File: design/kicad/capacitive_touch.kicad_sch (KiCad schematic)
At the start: 65 parts, among them J10 Conn_01x09_Pin, J2 Conn_01x09_Pin, J4 Conn_01x09_Socket, J5 Conn_01x09_Socket, J6 Conn_01x09_Socket, J7 Conn_01x09_Socket, J8 Conn_01x09_Pin, J9 Conn_01x09_Pin, U4 MPR121QR2, U5 MPR121QR2, U6 MPR121QR2

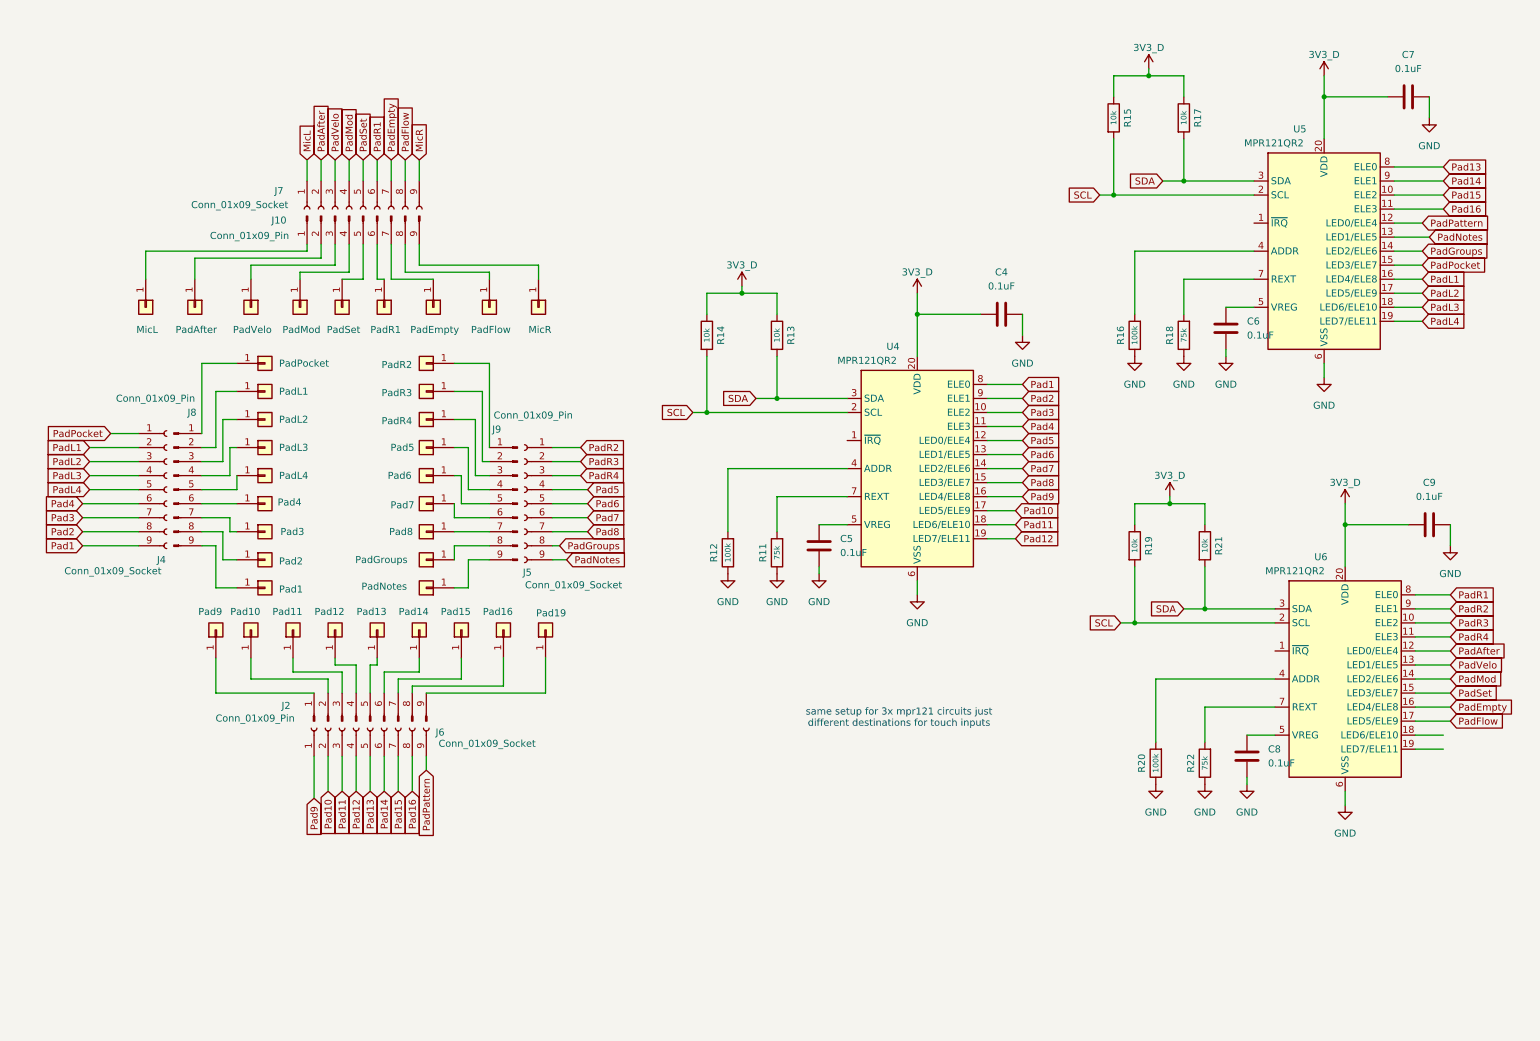
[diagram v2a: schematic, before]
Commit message: completes kicad schematic, starts pcb layout
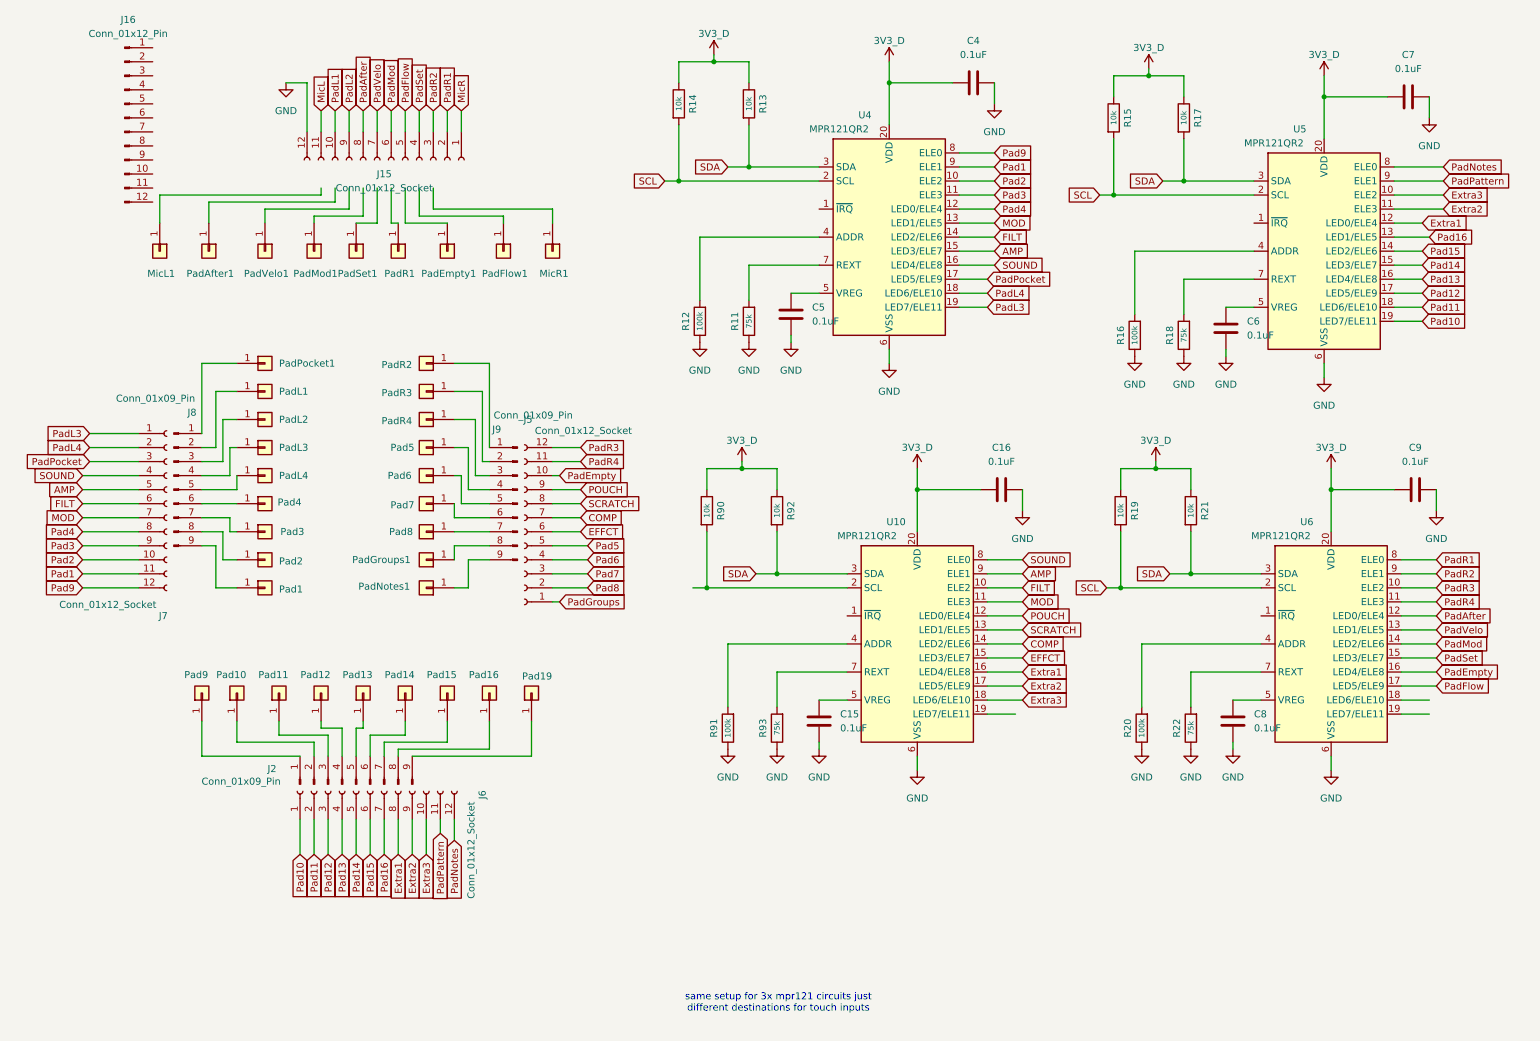
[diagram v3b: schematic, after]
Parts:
- removed J10: Conn_01x09_Pin, symbol Connector:Conn_01x09_Pin
- removed J4, J5, J6, J7: Conn_01x09_Socket, symbol Connector:Conn_01x09_Socket
- added C15, C16: 0.1uF, Capacitor_SMD:C_0402_1005Metric, symbol Device:C
- added J15, J5, J6, J7: Conn_01x12_Socket, Connector_PinSocket_1.27mm:PinSocket_1x12_P1.27mm_Vertical, symbol Connector:Conn_01x12_Socket
- added J16: Conn_01x12_Pin, Connector_PinHeader_1.27mm:PinHeader_1x12_P1.27mm_Vertical_SMD_Pin1Left, symbol Connector:Conn_01x12_Pin
- added R90, R92: 10k, Resistor_SMD:R_0603_1608Metric, symbol Device:R
- added R91: 100k, Resistor_SMD:R_0603_1608Metric, symbol Device:R
- added R93: 75k, Resistor_SMD:R_0603_1608Metric, symbol Device:R
- added U10: MPR121QR2, Package_DFN_QFN:UQFN-20_3x3mm_P0.4mm, symbol Sensor_Touch:MPR121QR2
- C4, C7, C9: footprint Capacitor_SMD:C_0603_1608Metric -> Capacitor_SMD:C_0402_1005Metric; LCSC (none) -> C1525
- C5, C6, C8: footprint Capacitor_SMD:C_0603_1608Metric -> Capacitor_SMD:C_0402_1005Metric; LCSC C6119867 -> C1525
- J2, J8, J9: footprint (none) -> Connector_PinHeader_1.27mm:PinHeader_1x09_P1.27mm_Vertical_SMD_Pin1Left
- MicL1: renamed from MicL; footprint (none) -> TestPoint:TestPoint_Pad_2.5x2.5mm
- MicR1: renamed from MicR; footprint (none) -> TestPoint:TestPoint_Pad_2.5x2.5mm
- Pad1, Pad10, Pad11, Pad12, Pad13, Pad14, Pad15, Pad16, Pad19, Pad2, Pad3, Pad4, Pad5, Pad6, Pad7, Pad8, Pad9, PadL1, PadL2, PadL3, PadL4, PadR1, PadR2, PadR3, PadR4: footprint (none) -> TestPoint:TestPoint_Pad_2.5x2.5mm
- PadAfter1: renamed from PadAfter; footprint (none) -> TestPoint:TestPoint_Pad_2.5x2.5mm
- PadEmpty1: renamed from PadEmpty; footprint (none) -> TestPoint:TestPoint_Pad_2.5x2.5mm
- PadFlow1: renamed from PadFlow; footprint (none) -> TestPoint:TestPoint_Pad_2.5x2.5mm
- PadGroups1: renamed from PadGroups; footprint (none) -> TestPoint:TestPoint_Pad_2.5x2.5mm
- PadMod1: renamed from PadMod; footprint (none) -> TestPoint:TestPoint_Pad_2.5x2.5mm
- PadNotes1: renamed from PadNotes; footprint (none) -> TestPoint:TestPoint_Pad_2.5x2.5mm
- PadPocket1: renamed from PadPocket; footprint (none) -> TestPoint:TestPoint_Pad_2.5x2.5mm
- PadSet1: renamed from PadSet; footprint (none) -> TestPoint:TestPoint_Pad_2.5x2.5mm
- PadVelo1: renamed from PadVelo; footprint (none) -> TestPoint:TestPoint_Pad_2.5x2.5mm
- R11: LCSC C2907088 -> (none)
- U4, U5, U6: LCSC (none) -> C91322
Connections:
- net 3V3_D: now also C16.2, R90.1, R92.1, U10.20 (VDD)
- net GND: now also C15.1, C16.1, J15.12 (Pin_12), R91.1, R93.1, U10.6 (VSS)
- net MicL: now also J15.11 (Pin_11)
- net MicR: now also J15.1 (Pin_1)
- net Pad1: now also U4.9 (ELE1), J7.11 (Pin_11); no longer U4.8 (ELE0)
- net Pad10: now also U5.19 (LED7/ELE11), J6.1 (Pin_1); no longer U4.17 (LED5/ELE9)
- net Pad11: now also U5.18 (LED6/ELE10), J6.2 (Pin_2); no longer U4.18 (LED6/ELE10)
- net Pad12: now also U5.17 (LED5/ELE9), J6.3 (Pin_3); no longer U4.19 (LED7/ELE11)
- net Pad13: now also U5.16 (LED4/ELE8), J6.4 (Pin_4); no longer U5.8 (ELE0)
- net Pad14: now also U5.15 (LED3/ELE7), J6.5 (Pin_5); no longer U5.9 (ELE1)
- net Pad15: now also U5.14 (LED2/ELE6), J6.6 (Pin_6); no longer U5.10 (ELE2)
- net Pad16: now also U5.13 (LED1/ELE5), J6.7 (Pin_7); no longer U5.11 (ELE3)
- net Pad2: now also U4.10 (ELE2), J7.10 (Pin_10); no longer U4.9 (ELE1)
- net Pad3: now also U4.11 (ELE3), J7.9 (Pin_9); no longer U4.10 (ELE2)
- net Pad4: now also U4.12 (LED0/ELE4), J7.8 (Pin_8); no longer U4.11 (ELE3)
- net Pad5: now also J5.5 (Pin_5); no longer U4.12 (LED0/ELE4)
- net Pad6: now also J5.4 (Pin_4); no longer U4.13 (LED1/ELE5)
- net Pad7: now also J5.3 (Pin_3); no longer U4.14 (LED2/ELE6)
- net Pad8: now also J5.2 (Pin_2); no longer U4.15 (LED3/ELE7)
- net Pad9: now also U4.8 (ELE0), J7.12 (Pin_12); no longer U4.16 (LED4/ELE8)
- net PadAfter: now also J15.8 (Pin_8)
- net PadEmpty: now also J5.10 (Pin_10)
- net PadFlow: now also J15.5 (Pin_5)
- net PadGroups: now also J5.1 (Pin_1); no longer U5.14 (LED2/ELE6)
- net PadL1: now also J15.10 (Pin_10); no longer U5.16 (LED4/ELE8)
- net PadL2: now also J15.9 (Pin_9); no longer U5.17 (LED5/ELE9)
- net PadL3: now also U4.19 (LED7/ELE11), J7.1 (Pin_1); no longer U5.18 (LED6/ELE10)
- net PadL4: now also U4.18 (LED6/ELE10), J7.2 (Pin_2); no longer U5.19 (LED7/ELE11)
- net PadMod: now also J15.6 (Pin_6)
- net PadNotes: now also U5.8 (ELE0), J6.12 (Pin_12); no longer U5.13 (LED1/ELE5)
- net PadPattern: now also U5.9 (ELE1), J6.11 (Pin_11); no longer U5.12 (LED0/ELE4)
- net PadPocket: now also U4.17 (LED5/ELE9), J7.3 (Pin_3); no longer U5.15 (LED3/ELE7)
- net PadR1: now also J15.2 (Pin_2)
- net PadR2: now also J15.3 (Pin_3)
- net PadR3: now also J5.12 (Pin_12)
- net PadR4: now also J5.11 (Pin_11)
- net PadSet: now also J15.4 (Pin_4)
- net PadVelo: now also J15.7 (Pin_7)
- net SDA: now also R92.2, U10.3 (SDA)
- new net: R91.2, U10.4 (ADDR)
- new net: R93.2, U10.7 (REXT)
- new net: R90.2, U10.2 (SCL)
- new net: C15.2, U10.5 (VREG)
- new net AMP: J7.5 (Pin_5), U10.9 (ELE1), U4.15 (LED3/ELE7)
- new net COMP: J5.7 (Pin_7), U10.14 (LED2/ELE6)
- new net EFFCT: J5.6 (Pin_6), U10.15 (LED3/ELE7)
- new net Extra1: J6.8 (Pin_8), U10.16 (LED4/ELE8), U5.12 (LED0/ELE4)
- new net Extra2: J6.9 (Pin_9), U10.17 (LED5/ELE9), U5.11 (ELE3)
- new net Extra3: J6.10 (Pin_10), U10.18 (LED6/ELE10), U5.10 (ELE2)
- new net FILT: J7.6 (Pin_6), U10.10 (ELE2), U4.14 (LED2/ELE6)
- new net MOD: J7.7 (Pin_7), U10.11 (ELE3), U4.13 (LED1/ELE5)
- new net POUCH: J5.9 (Pin_9), U10.12 (LED0/ELE4)
- new net SCRATCH: J5.8 (Pin_8), U10.13 (LED1/ELE5)
- new net SOUND: J7.4 (Pin_4), U10.8 (ELE0), U4.16 (LED4/ELE8)
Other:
- moved on the sheet: C4, C5, C8, C9, J2, MicL1, MicR1, Pad10, Pad11, Pad12, Pad13, Pad14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

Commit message: routes PCB all except PWR
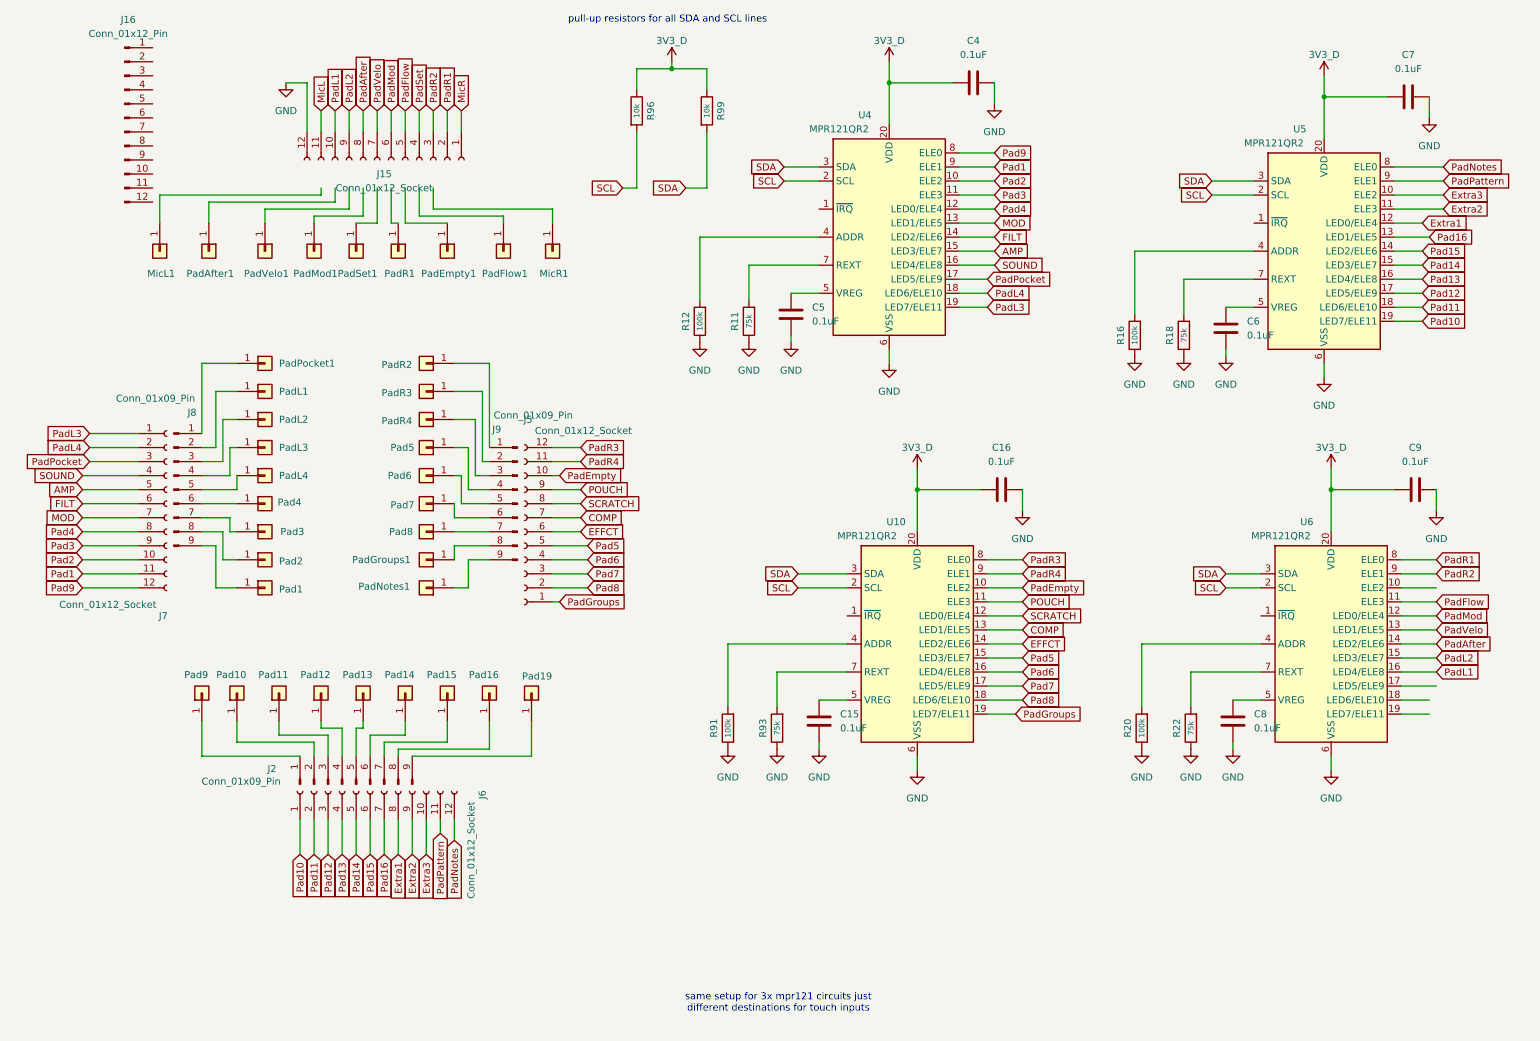
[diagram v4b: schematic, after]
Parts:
- removed R13, R14, R15, R17, R19, R21, R90, R92: 10k, Resistor_SMD:R_0603_1608Metric, symbol Device:R
- added R96, R99: 10k, Resistor_SMD:R_0603_1608Metric, symbol Device:R
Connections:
- net 3V3_D: now also R96.1, R99.1
- net AMP: no longer U10.9 (ELE1)
- net COMP: now also U10.13 (LED1/ELE5); no longer U10.14 (LED2/ELE6)
- net EFFCT: now also U10.14 (LED2/ELE6); no longer U10.15 (LED3/ELE7)
- net Extra1: no longer U10.16 (LED4/ELE8)
- net Extra2: no longer U10.17 (LED5/ELE9)
- net Extra3: no longer U10.18 (LED6/ELE10)
- net FILT: no longer U10.10 (ELE2)
- net MOD: no longer U10.11 (ELE3)
- net POUCH: now also U10.11 (ELE3); no longer U10.12 (LED0/ELE4)
- net Pad5: now also U10.15 (LED3/ELE7)
- net Pad6: now also U10.16 (LED4/ELE8)
- net Pad7: now also U10.17 (LED5/ELE9)
- net Pad8: now also U10.18 (LED6/ELE10)
- net PadAfter: now also U6.14 (LED2/ELE6); no longer U6.12 (LED0/ELE4)
- net PadEmpty: now also U10.10 (ELE2); no longer U6.16 (LED4/ELE8)
- net PadFlow: now also U6.11 (ELE3); no longer U6.17 (LED5/ELE9)
- net PadGroups: now also U10.19 (LED7/ELE11)
- net PadL1: now also U6.16 (LED4/ELE8)
- net PadL2: now also U6.15 (LED3/ELE7)
- net PadMod: now also U6.12 (LED0/ELE4); no longer U6.14 (LED2/ELE6)
- net PadR3: now also U10.8 (ELE0); no longer U6.10 (ELE2)
- net PadR4: now also U10.9 (ELE1); no longer U6.11 (ELE3)
- net PadSet: no longer U6.15 (LED3/ELE7)
- net SCL: now also U10.2 (SCL), R96.2
- net SCRATCH: now also U10.12 (LED0/ELE4); no longer U10.13 (LED1/ELE5)
- net SDA: now also R99.2
- net SOUND: no longer U10.8 (ELE0)
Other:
- note added: "pull-up resistors for all SDA and SCL lines"
